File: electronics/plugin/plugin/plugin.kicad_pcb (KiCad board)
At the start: 2 copper layers, 10 x 13 mm, 10 parts, among them J1 Conn_01x01, J2 Conn_01x01, J3 Conn_01x02, Q2 Q_NMOS_DSG

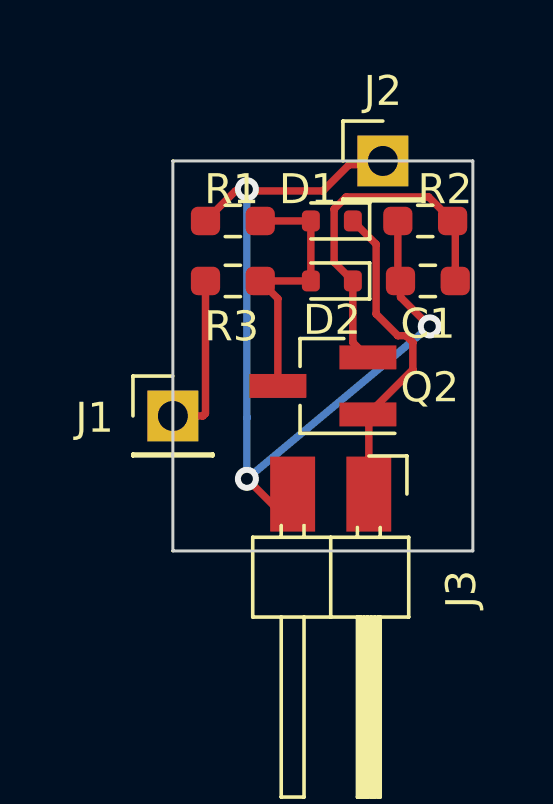
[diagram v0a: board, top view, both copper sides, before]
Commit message: plugin: Fix protection, notes on solder test and JFET amp setup
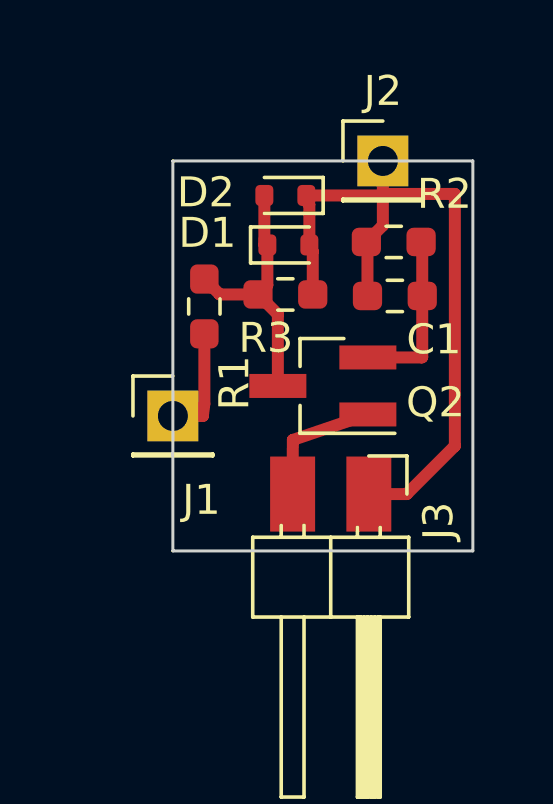
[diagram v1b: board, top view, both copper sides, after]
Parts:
- moved D2 3.24 mm to (48.8, 43.6)
- moved R3 3.01 mm to (48.8, 47.0), turned to 0 degrees
- moved D1 1.66 mm to (48.9, 45.3), turned to 0 degrees
- moved R1 1.27 mm to (46.0, 47.4), turned to 90 degrees
- moved R2 1.26 mm to (52.4, 45.2)
- moved C1 1.21 mm to (52.4, 47.0)
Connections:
- C1 pad 1: Net-(D2-K) -> Net-(Q2-S)
- D1 pad 1: /OUT -> /GATE
- D1 pad 2: Net-(D1-A) -> GND
- D2 pad 1: Net-(D2-K) -> GND
- D2 pad 2: Net-(D1-A) -> /GATE
- J3 pad 1: /OUT -> GND
- J3 pad 2: GND -> /OUT
- Q2 pad 2: Net-(D2-K) -> Net-(Q2-S)
- Q2 pad 3: Net-(D1-A) -> /GATE
- R1 pad 2: Net-(D1-A) -> /GATE
- R2 pad 1: Net-(D2-K) -> Net-(Q2-S)
- R3 pad 1: Net-(D1-A) -> /GATE
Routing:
- net Net-(D2-K): track 11.9 -> 0.00 mm
- net Net-(D1-A): track 9.12 -> 0.00 mm
- net /GATE: track 0.00 -> 8.60 mm
- net GND: track 30.3 -> 24.6 mm, vias 3 -> 0
- net /OUT: track 10.7 -> 5.04 mm
- net Net-(Q2-S): track 0.00 -> 5.67 mm
- net Net-(J1-Pin_1): track 5.41 -> 3.54 mm

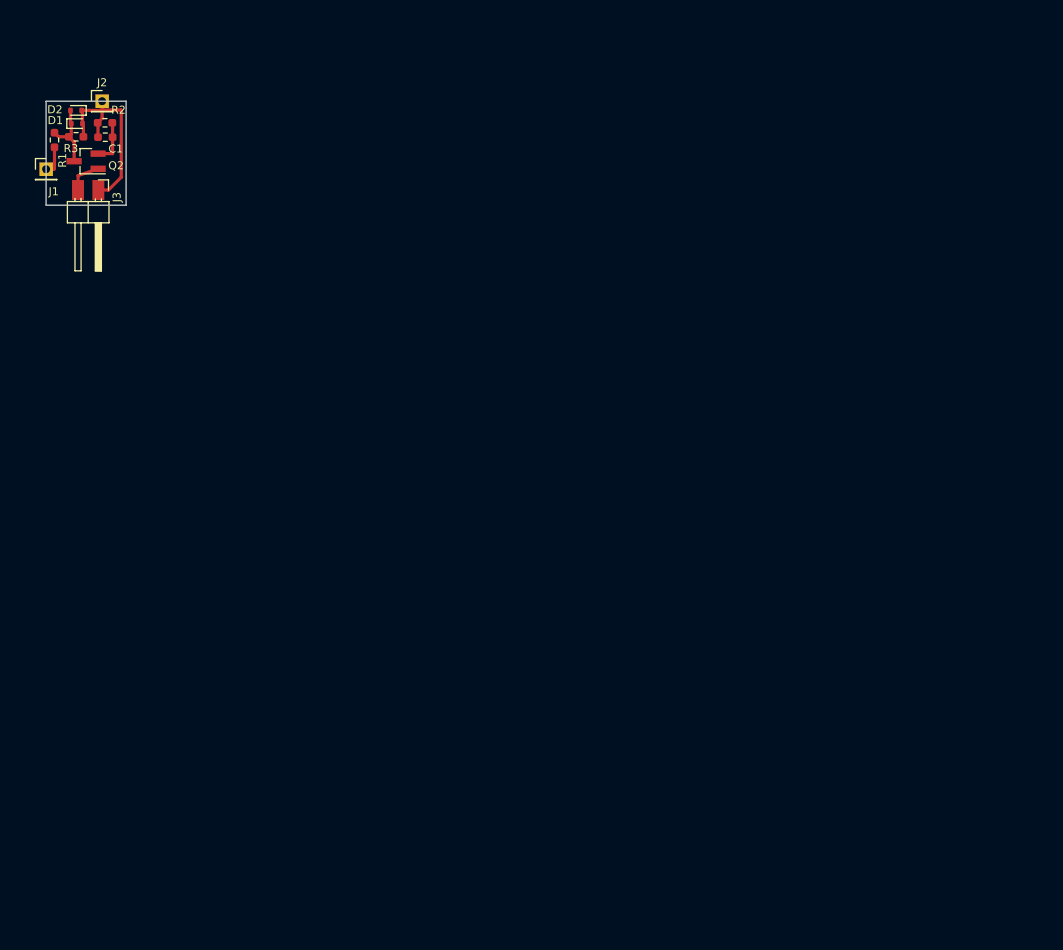
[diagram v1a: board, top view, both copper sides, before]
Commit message: Add some notes on PIP and a separate battery-powered preamp
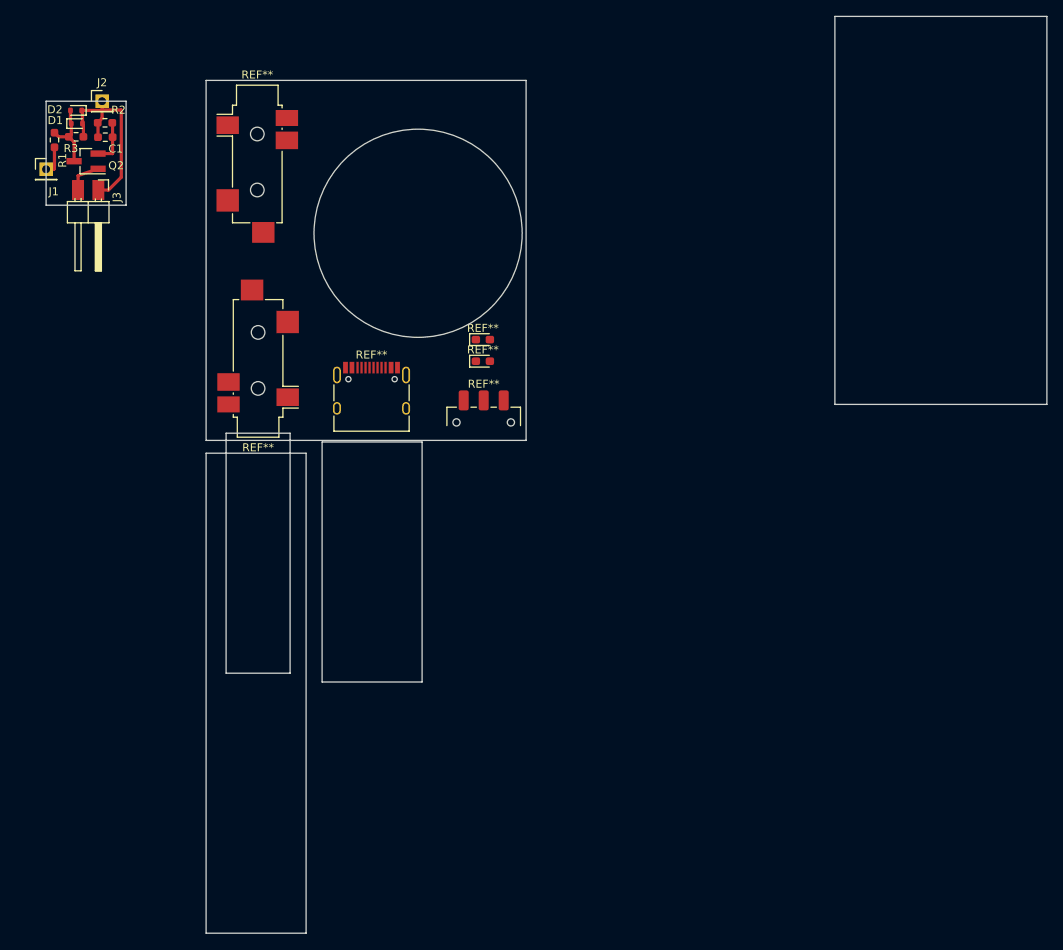
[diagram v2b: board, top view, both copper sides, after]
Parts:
- added REF**: USB_C_Receptacle_HRO_TYPE-C-31-M-12, Connector_USB:USB_C_Receptacle_HRO_TYPE-C-31-M-12, F.Cu at (85.7, 79.8)
- added REF**: SW_SPDT_CK_JS102011SAQN, Button_Switch_SMD:SW_SPDT_CK_JS102011SAQN, F.Cu at (99.7, 82.7)
- added REF**: LED_0603_1608Metric_Pad1.05x0.95mm_HandSolder, LED_SMD:LED_0603_1608Metric_Pad1.05x0.95mm_HandSolder, F.Cu at (99.6, 72.3)
- added REF**: LED_0603_1608Metric_Pad1.05x0.95mm_HandSolder, LED_SMD:LED_0603_1608Metric_Pad1.05x0.95mm_HandSolder, F.Cu at (99.6, 75.0)
- added REF**: Jack_3.5mm_CUI_SJ2-3593D-SMT_Horizontal, Connector_Audio:Jack_3.5mm_CUI_SJ2-3593D-SMT_Horizontal, F.Cu at (71.5, 75.9)
- added REF**: Jack_3.5mm_CUI_SJ2-3593D-SMT_Horizontal, Connector_Audio:Jack_3.5mm_CUI_SJ2-3593D-SMT_Horizontal, F.Cu at (71.4, 49.1)
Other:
- board size 10 x 13 mm -> 125.1 x 114.6 mm
- board text added: "Alternative to power switch: Audio jack detect switch"
- board text added: "LED indicator: power. LED indicator: charging"
- board text added: "LIR2450"
